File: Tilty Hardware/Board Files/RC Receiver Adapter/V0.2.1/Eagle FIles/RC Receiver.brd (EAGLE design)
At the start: 38.1 x 50.8 mm, 30 parts, among them U1 ATMEGA328P, U2 LM2931, U3 AP7313SOT23R, Y1 16MHz

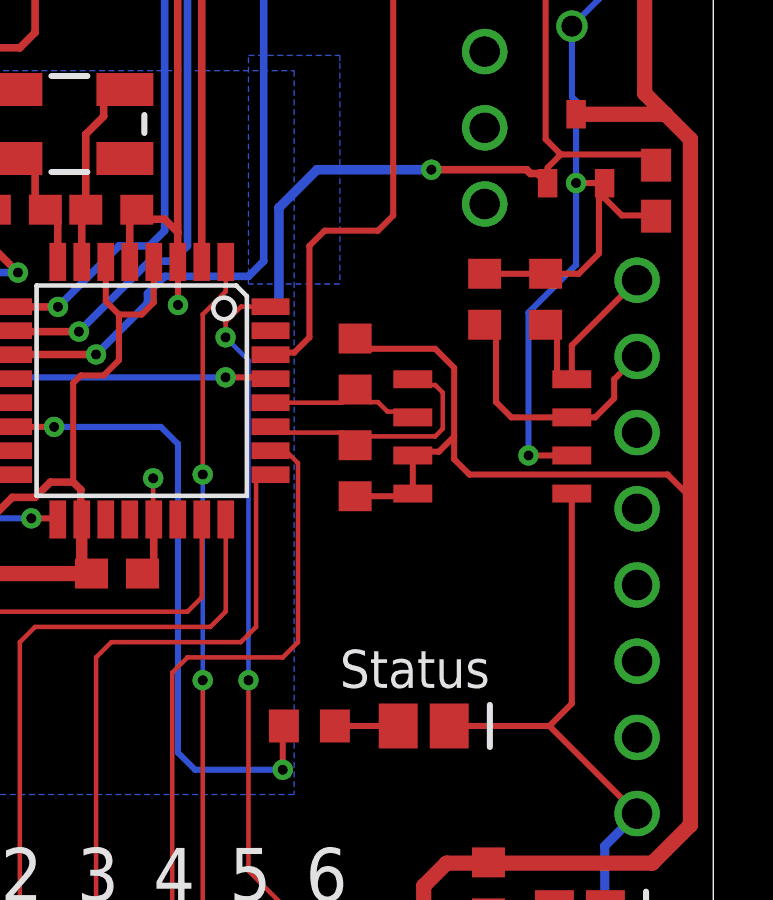
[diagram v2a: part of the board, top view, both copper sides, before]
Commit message: Added solder jumper to disable I2C level translation
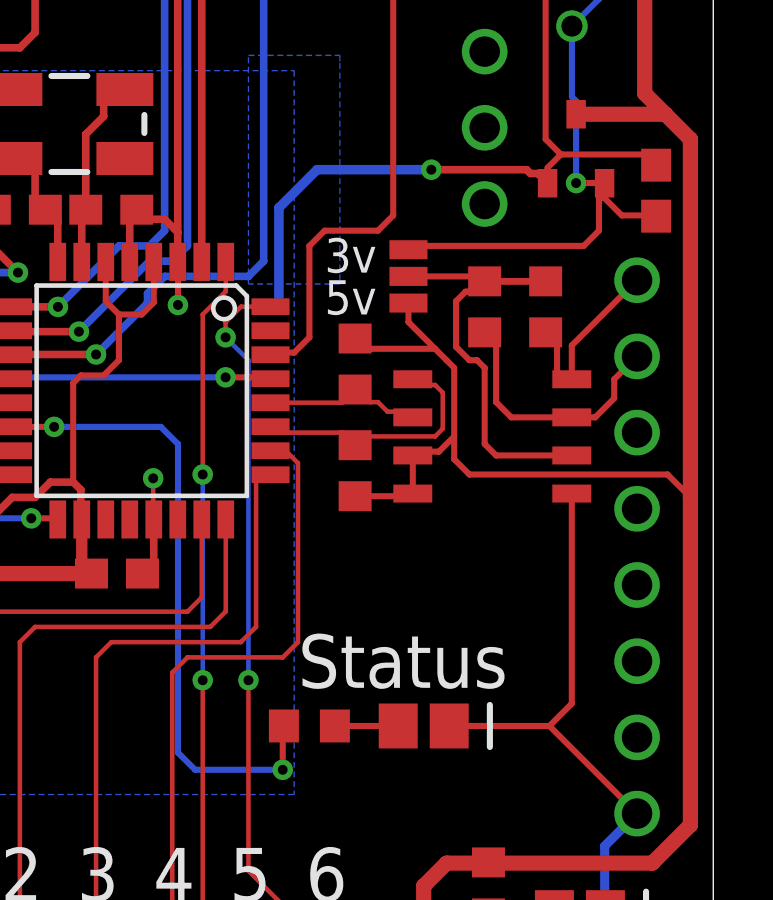
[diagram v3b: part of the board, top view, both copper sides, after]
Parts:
- added SJ2: (no value), SparkFun-Passives:SJ_3
- moved R6 0.25 mm to (30.5, 28.2)
- moved R7 0.25 mm to (32.5, 28.2)
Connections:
- new net N$7: R6.2, R7.2, SJ2.2, U$1.P$2
- net +3V3: now also SJ2.1; no longer R6.2, R7.2, U$1.P$2
- net +5V: now also SJ2.3
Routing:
- net N$7: track 0.00 -> 16.8 mm
- net +3V3: track 62.4 -> 53.0 mm, vias 2 -> 1
- net +5V: track 168.5 -> 170.4 mm
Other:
- board text added: "3v"
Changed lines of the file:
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@@
 <text x="27.178" y="45.974" size="1.778" layer="25" ratio="12">+</text>
 <text x="27.178" y="43.434" size="1.778" layer="25" ratio="12">S</text>
-<text x="25.654" y="15.494" size="1.27" layer="25" ratio="15">Status</text>
+<text x="24.257" y="15.494" size="1.778" layer="25" ratio="15">Status</text>
 <rectangle x1="22.866453125" y1="30.4422375" x2="23.008690625" y2="30.46255625" layer="26" rot="R213.3"/>
 <rectangle x1="22.834971875" y1="30.459221875" x2="23.017853125" y2="30.479540625" layer="26" rot="R213.3"/>
@@
 <text x="11.938" y="48.768" size="1.27" layer="26" ratio="15" rot="MR0">3v3</text>
 <text x="35.56" y="45.72" size="1.27" layer="25" ratio="15" rot="R150">GND</text>
+<text x="25.146" y="27.94" size="1.143" layer="25" ratio="15">5v</text>
+<text x="25.146" y="29.337" size="1.143" layer="25" ratio="15">3v</text>
 </plain>
 <attributes>
@@
 <element name="R5" library="resistor" package="R0603" value="220" x="30.607" y="8.8265" smashed="yes" rot="R90"/>
 <element name="U$1" library="My Parts" package="SOIC-8" value="PCA9306" x="30.734" y="23.876" rot="R180"/>
-<element name="R6" library="resistor" package="R0603" value="" x="30.48" y="28.448" smashed="yes" rot="R90">
-<attribute name="VALUE" x="32.512" y="27.559" size="1.27" layer="27" rot="R90"/>
+<element name="R6" library="resistor" package="R0603" value="" x="30.48" y="28.194" smashed="yes" rot="R90">
+<attribute name="VALUE" x="32.512" y="27.305" size="1.27" layer="27" rot="R90"/>
 </element>
-<element name="R7" library="resistor" package="R0603" value="" x="32.512" y="28.448" smashed="yes" rot="R90">
-<attribute name="VALUE" x="34.544" y="27.559" size="1.27" layer="27" rot="R90"/>
+<element name="R7" library="resistor" package="R0603" value="" x="32.512" y="28.194" smashed="yes" rot="R90">
+<attribute name="VALUE" x="34.544" y="27.305" size="1.27" layer="27" rot="R90"/>
+</element>
+<element name="SJ2" library="SparkFun-Passives" package="SJ_3" value="" x="27.94" y="29.21" smashed="yes" rot="R270">
+<attribute name="VALUE" x="27.94" y="29.3101" size="0.02" layer="27" rot="R270"/>
+<attribute name="VALUE" x="26.035" y="30.48" size="0.4064" layer="27" rot="R270"/>
 </element>
 </elements>
@@
 <wire x1="26.328" y1="27.139" x2="26.67" y2="26.797" width="0.2032" layer="1"/>
 <wire x1="26.67" y1="26.797" x2="28.829" y2="26.797" width="0.2032" layer="1"/>
-<wire x1="28.829" y1="26.797" x2="29.464" y2="26.162" width="0.2032" layer="1"/>
+<wire x1="28.829" y1="26.797" x2="29.21" y2="26.416" width="0.2032" layer="1"/>
+<wire x1="29.21" y1="26.416" x2="29.464" y2="26.162" width="0.2032" layer="1"/>
 <wire x1="29.464" y1="26.162" x2="29.464" y2="23.876" width="0.2032" layer="1"/>
 <wire x1="29.464" y1="23.876" x2="29.464" y2="23.114" width="0.2032" layer="1"/>
@@
 <wire x1="29.972" y1="22.606" x2="36.576" y2="22.606" width="0.2032" layer="1"/>
 <wire x1="36.576" y1="22.606" x2="37.338" y2="21.844" width="0.2032" layer="1"/>
+<contactref element="SJ2" pad="3"/>
+<wire x1="27.94" y1="28.321" x2="27.94" y2="27.686" width="0.2032" layer="1"/>
+<wire x1="27.94" y1="27.686" x2="28.829" y2="26.797" width="0.2032" layer="1"/>
 </signal>
 <signal name="N$5">
@@
 <wire x1="33.02" y1="45.593" x2="11.43" y2="45.593" width="0.254" layer="16"/>
 <wire x1="11.43" y1="45.593" x2="7.62" y2="49.403" width="0.254" layer="16"/>
-<contactref element="U$1" pad="P$2"/>
-<contactref element="R7" pad="2"/>
-<contactref element="R6" pad="2"/>
-<wire x1="30.48" y1="29.298" x2="32.512" y2="29.298" width="0.2032" layer="1"/>
-<via x="31.9405" y="23.241" extent="1-16" drill="0.3302"/>
-<wire x1="31.9405" y1="23.241" x2="33.384" y2="23.241" width="0.2032" layer="1"/>
-<wire x1="31.9405" y1="23.241" x2="31.9405" y2="28.0035" width="0.2032" layer="16"/>
 <wire x1="34.478" y1="32.3145" x2="34.478" y2="31.816" width="0.2032" layer="1"/>
 <wire x1="34.478" y1="31.816" x2="35.052" y2="31.242" width="0.2032" layer="1"/>
@@
 <wire x1="34.29" y1="44.704" x2="34.29" y2="38.454" width="0.2032" layer="16"/>
 <wire x1="34.29" y1="38.454" x2="33.3885" y2="37.5525" width="0.2032" layer="16"/>
-<wire x1="31.9405" y1="28.0035" x2="33.528" y2="29.591" width="0.2032" layer="16"/>
-<wire x1="33.528" y1="29.591" x2="33.528" y2="32.3215" width="0.2032" layer="16"/>
-<wire x1="32.512" y1="29.298" x2="33.616" y2="29.298" width="0.2032" layer="1"/>
-<wire x1="33.616" y1="29.298" x2="34.29" y2="29.972" width="0.2032" layer="1"/>
-<wire x1="34.29" y1="29.972" x2="34.29" y2="32.004" width="0.2032" layer="1"/>
+<contactref element="SJ2" pad="1"/>
+<wire x1="34.29" y1="32.004" x2="34.29" y2="30.734" width="0.2032" layer="1"/>
+<wire x1="34.29" y1="30.734" x2="33.782" y2="30.226" width="0.2032" layer="1"/>
+<wire x1="33.782" y1="30.226" x2="28.067" y2="30.226" width="0.2032" layer="1"/>
+<wire x1="28.067" y1="30.226" x2="27.94" y2="30.099" width="0.2032" layer="1"/>
 </signal>
 <signal name="SERVO_3">
@@
 <wire x1="33.384" y1="25.781" x2="33.384" y2="26.907" width="0.2032" layer="1"/>
 <wire x1="33.384" y1="26.907" x2="35.56" y2="29.083" width="0.2032" layer="1"/>
-<wire x1="32.512" y1="27.598" x2="32.512" y2="27.559" width="0.2032" layer="1"/>
+<wire x1="32.512" y1="27.344" x2="32.512" y2="27.559" width="0.2032" layer="1"/>
 <wire x1="32.512" y1="27.559" x2="32.8295" y2="27.2415" width="0.2032" layer="1"/>
 <wire x1="32.8295" y1="27.2415" x2="32.893" y2="27.2415" width="0.2032" layer="1"/>
-<wire x1="32.9565" y1="27.2415" x2="32.893" y2="27.2415" width="0.2032" layer="1"/>
+<wire x1="32.7025" y1="27.2415" x2="32.8295" y2="27.2415" width="0.2032" layer="1"/>
 <wire x1="32.893" y1="27.2415" x2="32.893" y2="25.908" width="0.2032" layer="1"/>
 <wire x1="32.893" y1="25.908" x2="33.257" y2="25.908" width="0.2032" layer="1"/>
@@
 <wire x1="31.369" y1="24.511" x2="30.861" y2="25.019" width="0.2032" layer="1"/>
 <wire x1="30.861" y1="25.019" x2="30.861" y2="27.217" width="0.2032" layer="1"/>
-<wire x1="30.861" y1="27.217" x2="30.48" y2="27.598" width="0.2032" layer="1"/>
+<wire x1="30.861" y1="27.217" x2="30.48" y2="27.344" width="0.2032" layer="1"/>
 </signal>
 <signal name="N$6">
@@
 <wire x1="25.488" y1="14.224" x2="27.598" y2="14.224" width="0.2032" layer="1"/>
 </signal>
+<signal name="N$7">
+<contactref element="R7" pad="2"/>
+<contactref element="R6" pad="2"/>
+<wire x1="30.48" y1="29.044" x2="30.988" y2="29.044" width="0.2032" layer="1"/>
+<contactref element="SJ2" pad="2"/>
+<wire x1="30.988" y1="29.044" x2="32.512" y2="29.044" width="0.2032" layer="1"/>
+<wire x1="27.94" y1="29.21" x2="30.822" y2="29.21" width="0.2032" layer="1"/>
+<wire x1="30.822" y1="29.21" x2="30.988" y2="29.044" width="0.2032" layer="1"/>
+<contactref element="U$1" pad="P$2"/>
+<wire x1="32.512" y1="29.044" x2="30.568" y2="29.044" width="0.2032" layer="1"/>
+<wire x1="30.568" y1="29.044" x2="30.48" y2="28.956" width="0.2032" layer="1"/>
+<wire x1="30.48" y1="28.956" x2="30.226" y2="28.956" width="0.2032" layer="1"/>
+<wire x1="30.226" y1="28.956" x2="29.972" y2="28.702" width="0.2032" layer="1"/>
+<wire x1="29.972" y1="28.702" x2="29.845" y2="28.702" width="0.2032" layer="1"/>
+<wire x1="29.845" y1="28.702" x2="29.5275" y2="28.3845" width="0.2032" layer="1"/>
+<wire x1="29.5275" y1="28.3845" x2="29.5275" y2="26.8605" width="0.2032" layer="1"/>
+<wire x1="29.5275" y1="26.8605" x2="29.972" y2="26.416" width="0.2032" layer="1"/>
+<wire x1="29.972" y1="26.416" x2="30.226" y2="26.416" width="0.2032" layer="1"/>
+<wire x1="30.226" y1="26.416" x2="30.48" y2="26.162" width="0.2032" layer="1"/>
+<wire x1="33.384" y1="23.241" x2="30.861" y2="23.241" width="0.2032" layer="1"/>
+<wire x1="30.861" y1="23.241" x2="30.48" y2="23.622" width="0.2032" layer="1"/>
+<wire x1="30.48" y1="23.622" x2="30.48" y2="26.162" width="0.2032" layer="1"/>
+</signal>
 </signals>

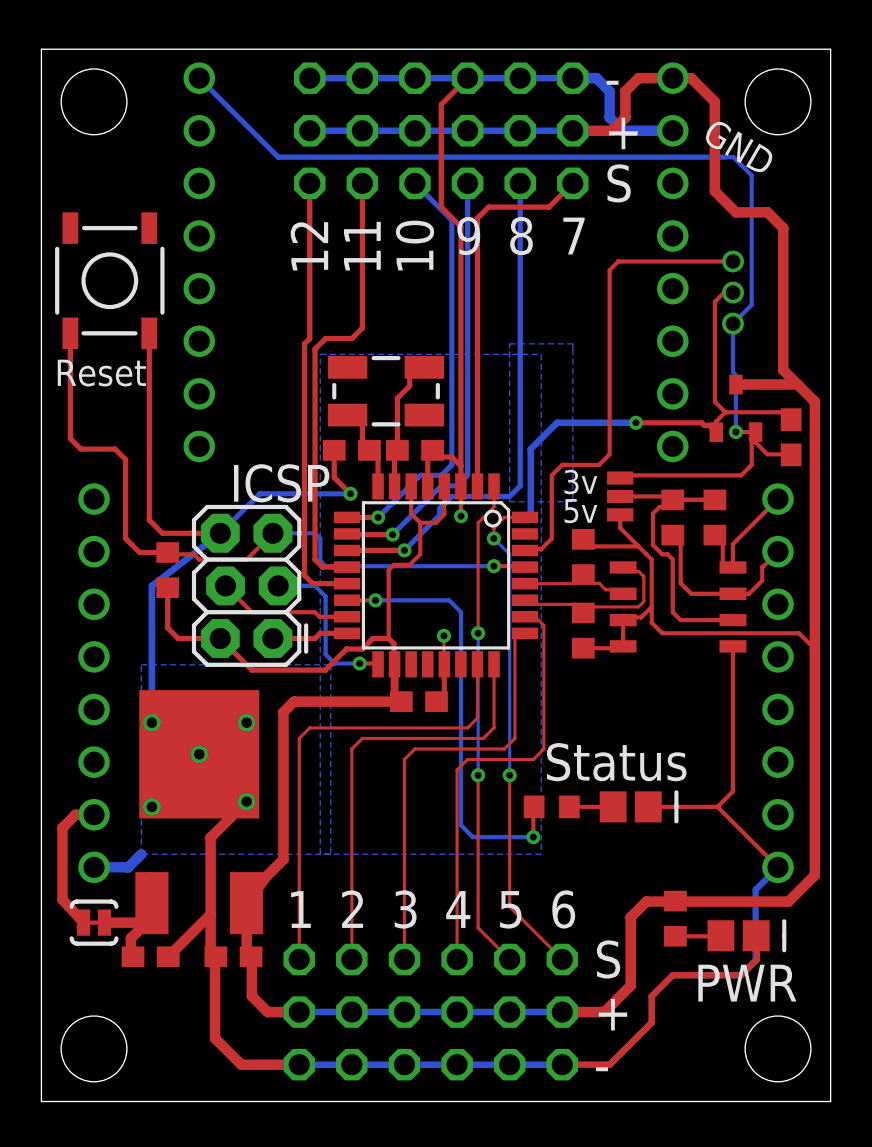
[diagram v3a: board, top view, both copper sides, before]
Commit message: Updated RC adapter
Changed to use locking headers, 3v3 I2C line with level
translator/buffer, moved LEDs
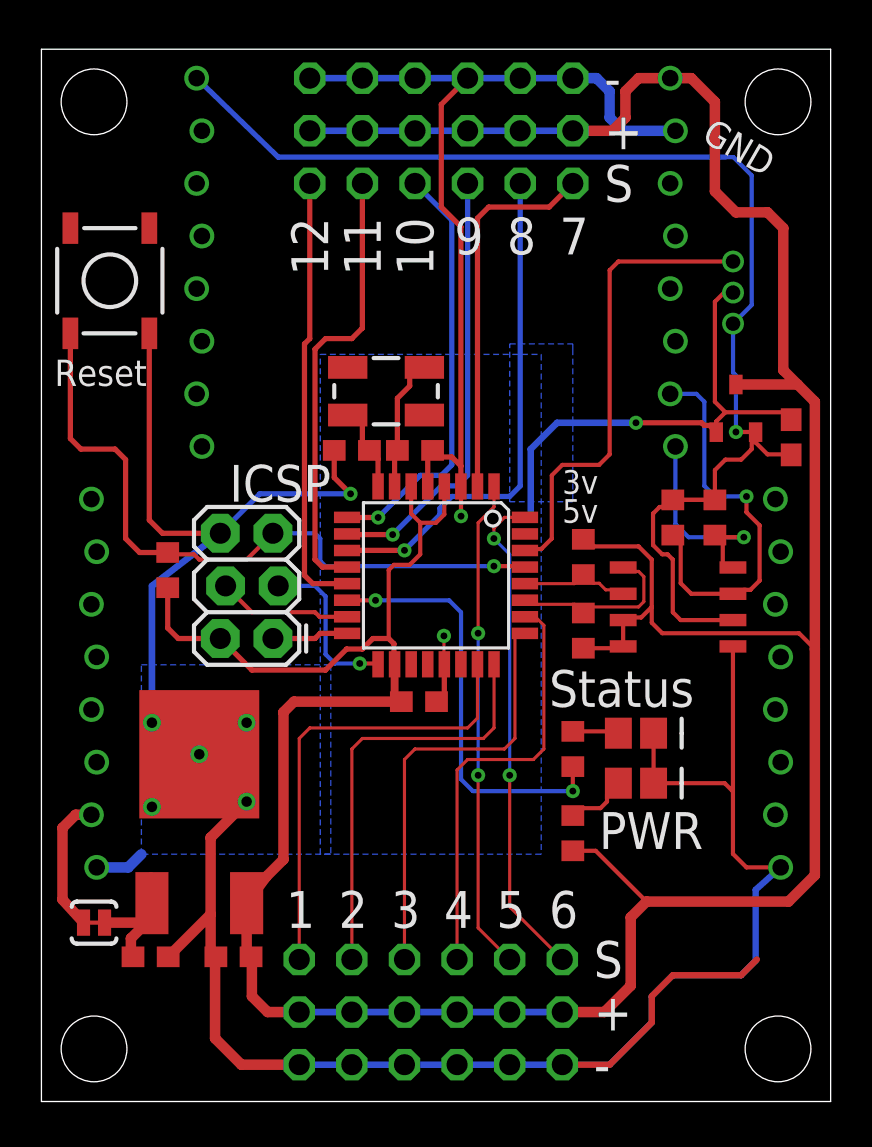
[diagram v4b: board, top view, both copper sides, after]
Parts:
- removed SJ2: (no value), SparkFun-Passives:SJ_3
- JP1, JP2, JP3, JP4: value (none) -> 8-PIN_HEADER; device pinhead:1X08_NO_SS -> My Parts:8-PIN_RECEPTACLE_LOCK_NO-SS
- moved D2 8.88 mm to (28.7, 15.4)
- moved R5 6.45 mm to (25.7, 13.0), turned to 270 degrees
- moved D1 3.57 mm to (28.7, 17.8)
- moved R4 2.97 mm to (25.7, 17.0), turned to 270 degrees
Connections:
- removed net N$7: R6.2, R7.2, SJ2.2, U$1.P$2
- net +3V3: now also JP1.P$8, R6.2, R7.2, U$1.P$2; no longer JP1.8, SJ2.1
- net +5V: now also JP4.P$8; no longer JP4.8, SJ2.3
- net 3V_SCL: now also JP4.P$2; no longer JP3.7
- net 3V_SDA: now also JP4.P$1; no longer JP3.8
- net GND: now also JP2.P$1, JP3.P$1, JP4.P$7; no longer JP2.1, JP3.1, JP4.7
- net N$5: now also JP2.P$2; no longer JP2.2
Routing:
- net N$7: track 16.8 -> 0.00 mm
- net 3V_SCL: track 8.72 -> 19.3 mm, vias 0 -> 1
- net +3V3: track 53.0 -> 63.2 mm
- net 3V_SDA: track 6.93 -> 11.5 mm, vias 0 -> 1
- net GND: track 186.1 -> 188.5 mm
- net +5V: track 170.4 -> 171.7 mm
- net N$4: track 2.21 -> 3.05 mm
- net STATUS_LED: track 21.2 -> 20.6 mm
